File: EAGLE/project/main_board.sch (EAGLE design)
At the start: 12 parts

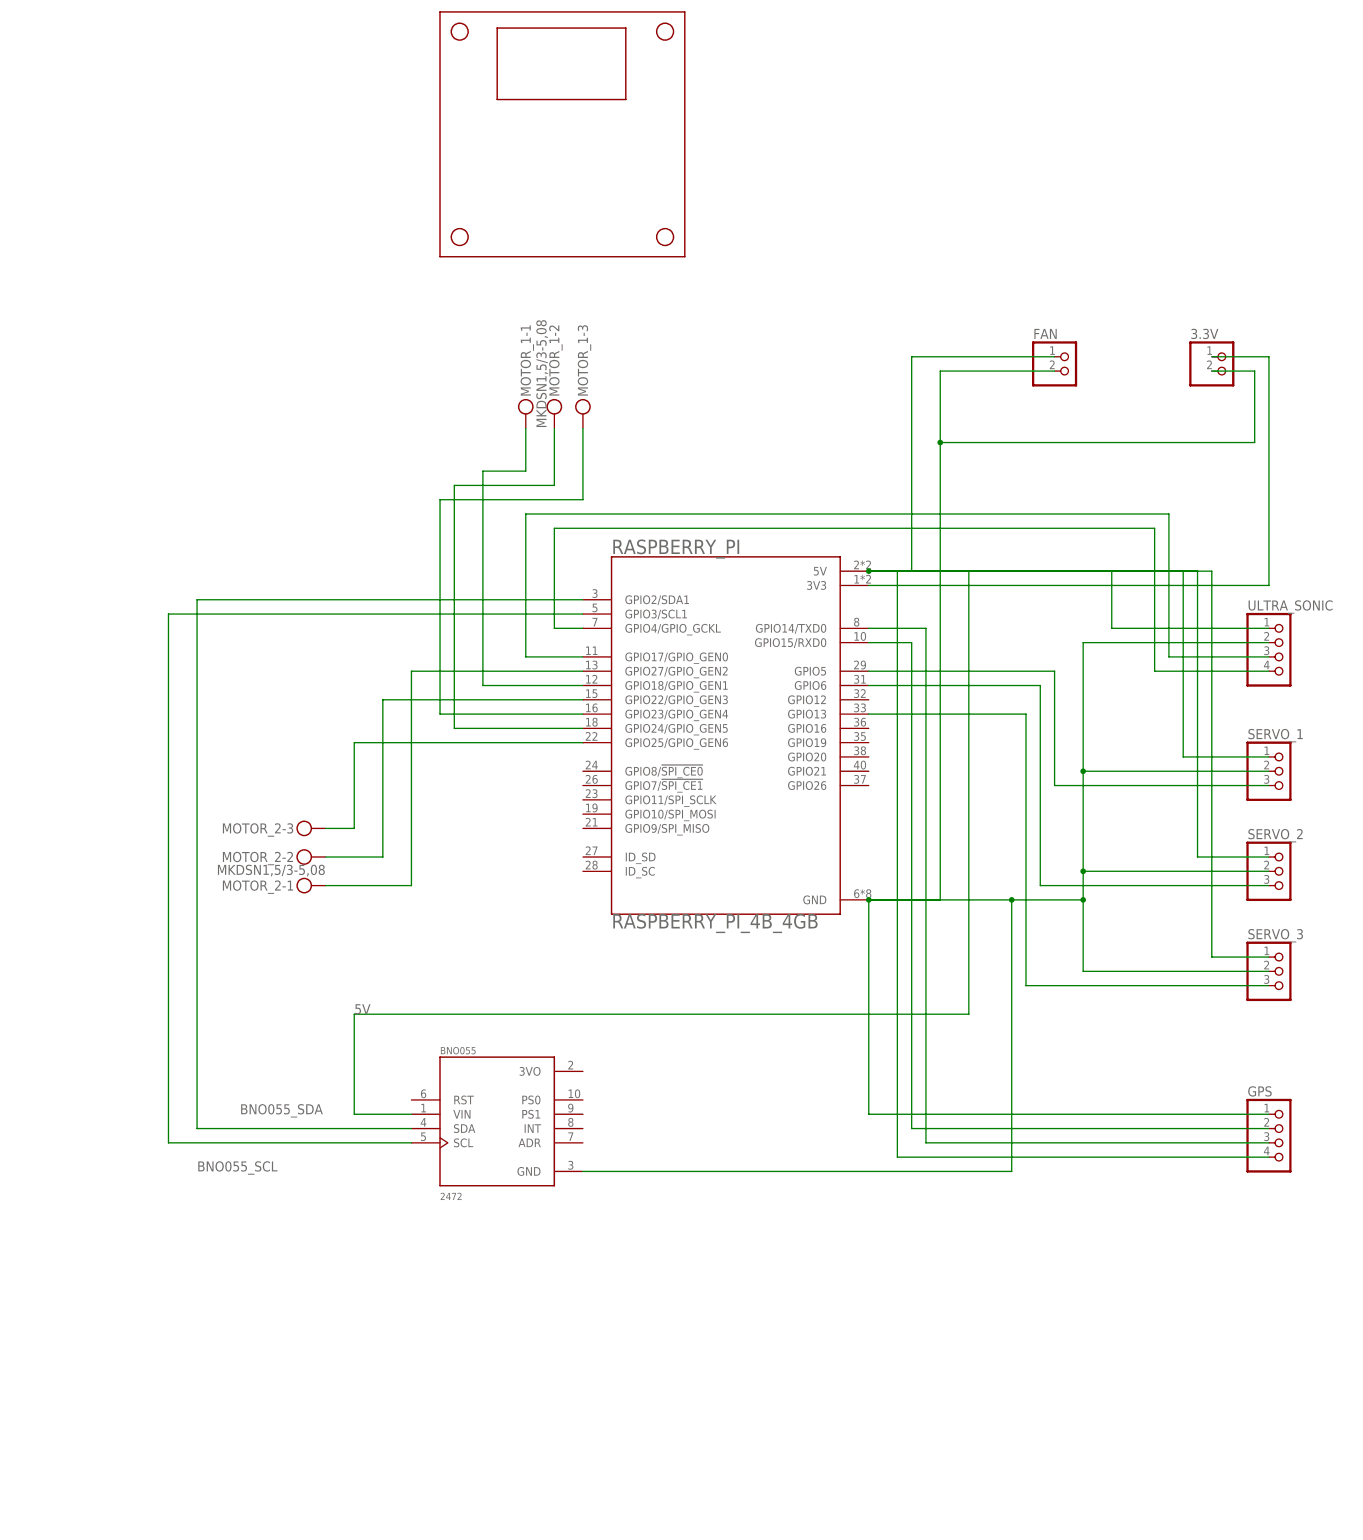
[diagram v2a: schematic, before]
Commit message: add communication and temp/humid sensor module
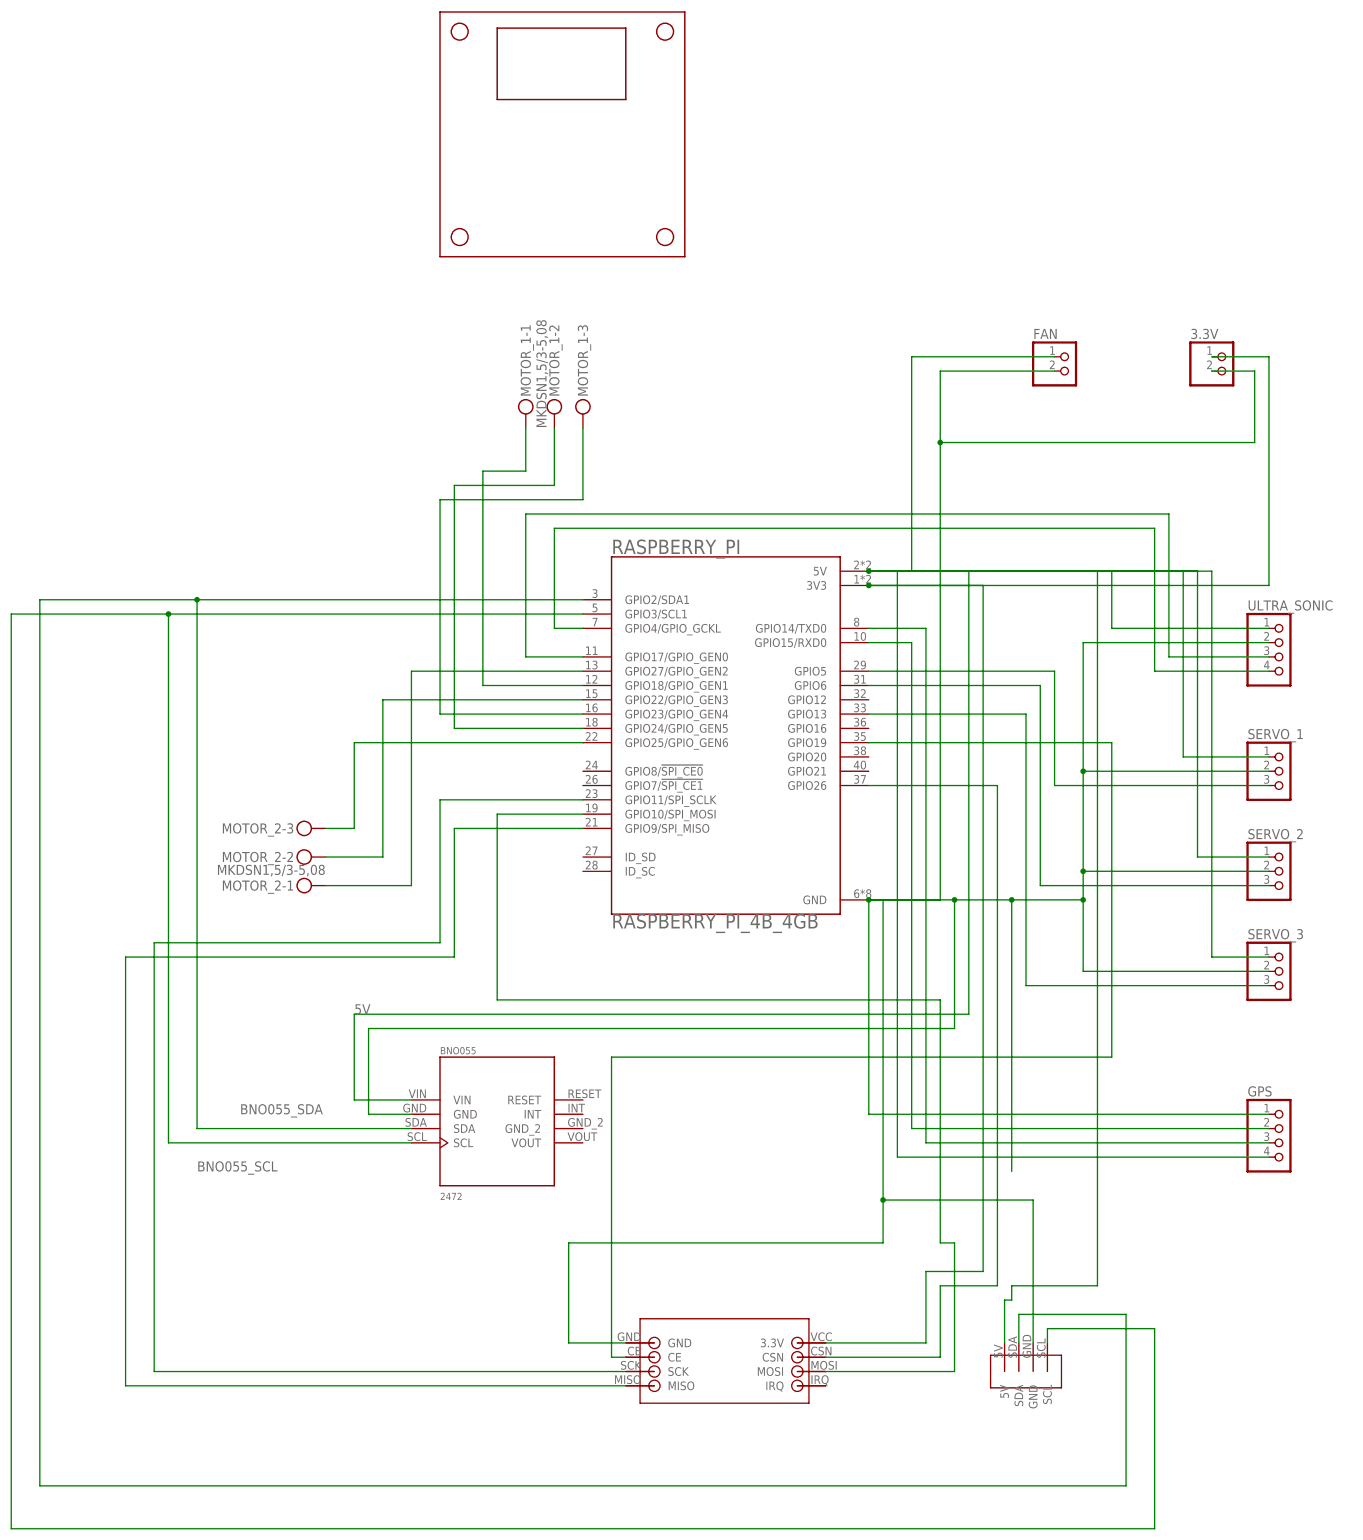
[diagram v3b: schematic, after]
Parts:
- added NRF24L1: NRF24L01, nRF24L01:NRF24L01
- added U$1: DHT20, DHT20:DHT20
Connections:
- new net N$1: NRF24L1.CE, RASPBERRY_PI.GPIO19
- new net N$2: NRF24L1.CSN, RASPBERRY_PI.GPIO26
- new net N$3: NRF24L1.SCK, RASPBERRY_PI.GPIO11/SPI_SCLK
- new net N$4: NRF24L1.MOSI, RASPBERRY_PI.GPIO10/SPI_MOSI
- new net N$5: NRF24L1.MISO, RASPBERRY_PI.GPIO9/SPI_MISO
- net 3.3V: now also NRF24L1.3.3V
- net 5V: now also U$1.5V
- net BNO055_SCL: now also U$1.SCL
- net BNO055_SDA: now also U$1.SDA
- net GND: now also NRF24L1.GND, U$1.GND
